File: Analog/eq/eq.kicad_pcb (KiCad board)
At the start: 2 copper layers, 39 parts, among them J2 NMJ4HCD2, J3 NMJ6HCD2, U1 NJM4580, U3 SA5532

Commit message: EQ pcb started and Analog file re-org
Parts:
- moved J3 70.9 mm to (72.6, 69.9)
- moved J2 38.7 mm to (179.6, 64.9)
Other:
- board text added: "INPUT"
- board text added: "OUTPUT"
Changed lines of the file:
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@@
 	(footprint "Connector_Audio:Jack_6.35mm_Neutrik_NMJ6HCD2_Horizontal"
 		(layer "F.Cu")
-		(at 143.385 72.305)
+		(at 72.565 69.885)
 		(descr "M Series, 6.35mm (1/4in) stereo jack, switched, with chrome ferrule and straight PCB pins, https://www.neutrik.com/en/product/nmj6hcd2")
 		(tags "neutrik jack m")
@@
 	(footprint "Connector_Audio:Jack_6.35mm_Neutrik_NMJ4HCD2_Horizontal"
 		(layer "F.Cu")
-		(at 143.385 51.025)
+		(at 179.565 64.885)
 		(descr "M Series, 6.35mm (1/4in) mono jack, switched, with chrome ferrule and straight PCB pins, https://www.neutrik.com/en/product/nmj4hcd2")
 		(tags "neutrik jack m")
@@
 		)
 	)
+	(gr_text "INPUT"
+		(at 78 64 0)
+		(layer "F.SilkS")
+		(effects
+			(font
+				(size 1 1)
+				(thickness 0.1)
+			)
+			(justify left bottom)
+		)
+	)
+	(gr_text "OUTPUT"
+		(at 183 59 0)
+		(layer "F.SilkS")
+		(effects
+			(font
+				(size 1 1)
+				(thickness 0.1)
+			)
+			(justify left bottom)
+		)
+	)

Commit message: EQ pcb done
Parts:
- added BT1: Battery, Connector_PinHeader_2.54mm:PinHeader_1x02_P2.54mm_Vertical, F.Cu at (233.7, 154.6)
- moved R1 157.4 mm to (226.0, 145.0), turned to 180 degrees
- moved R3 146.9 mm to (215.8, 149.0)
- moved R5 146.2 mm to (226.0, 141.0), turned to 180 degrees
- moved R2 144.0 mm to (212.5, 144.5), turned to 180 degrees
- moved HIGH1 137.7 mm to (247.9, 112.4), turned to 90 degrees
- moved R15 137.3 mm to (236.7, 120.8)
- moved R11 130.9 mm to (226.1, 126.5), turned to 180 degrees
- moved R14 129.6 mm to (226.1, 133.5), turned to 180 degrees
- moved R4 123.2 mm to (200.6, 134.0), turned to 180 degrees
- moved J3 121.0 mm to (170.4, 141.1), turned to 180 degrees
- moved R13 119.9 mm to (215.9, 130.0)
- moved D1 119.0 mm to (229.5, 144.9), turned to -90 degrees
- moved R8 118.7 mm to (196.6, 148.0), turned to 180 degrees
- moved R9 111.2 mm to (200.6, 130.5), turned to 180 degrees
- moved RPD1 108.7 mm to (202.3, 148.0)
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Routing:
- net Net-(C7-Pad2): track 0.00 -> 113.5 mm
- net Net-(C9-Pad1): track 0.00 -> 68.9 mm
- net Net-(C4-Pad2): track 0.00 -> 60.5 mm
- net VB: track 0.00 -> 60.0 mm
- net Net-(C2-Pad2): track 0.00 -> 58.9 mm
- net Net-(C8-Pad1): track 0.00 -> 53.5 mm
- net Net-(C11-Pad2): track 0.00 -> 46.0 mm
- net VA: track 0.00 -> 44.0 mm
- net Net-(C13-Pad2): track 0.00 -> 35.6 mm
- net Net-(C12-Pad1): track 0.00 -> 30.9 mm
- net Net-(C14-Pad1): track 0.00 -> 26.4 mm
- net Net-(C10-Pad2): track 0.00 -> 26.2 mm
- net Net-(C5-Pad2): track 0.00 -> 25.9 mm
- net Net-(U1A--): track 0.00 -> 24.5 mm
- net Net-(C15-Pad2): track 0.00 -> 23.9 mm
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- added copper zone on B.Cu, net GND
- added copper zone on F.Cu, net GND
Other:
- board outline added: 100 x 69 mm

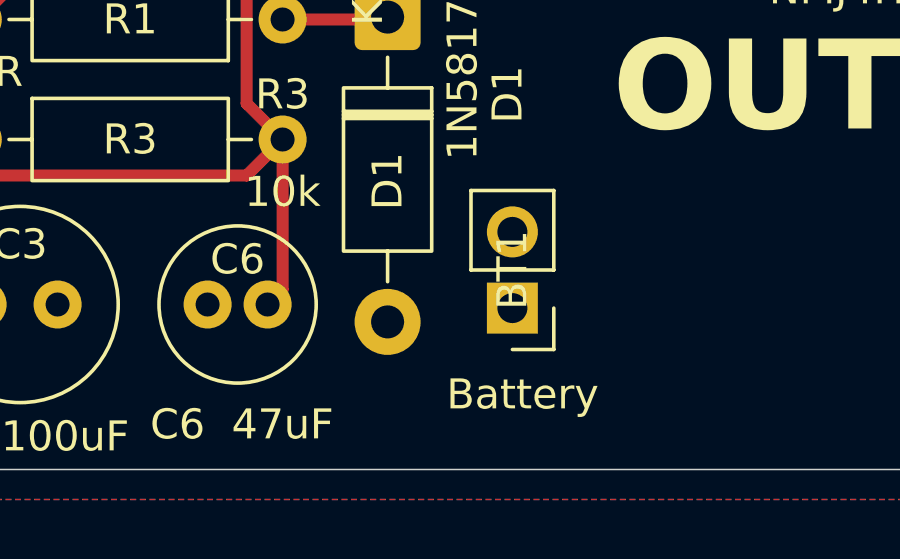
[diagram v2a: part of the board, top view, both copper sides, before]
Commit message: fixed battery trace
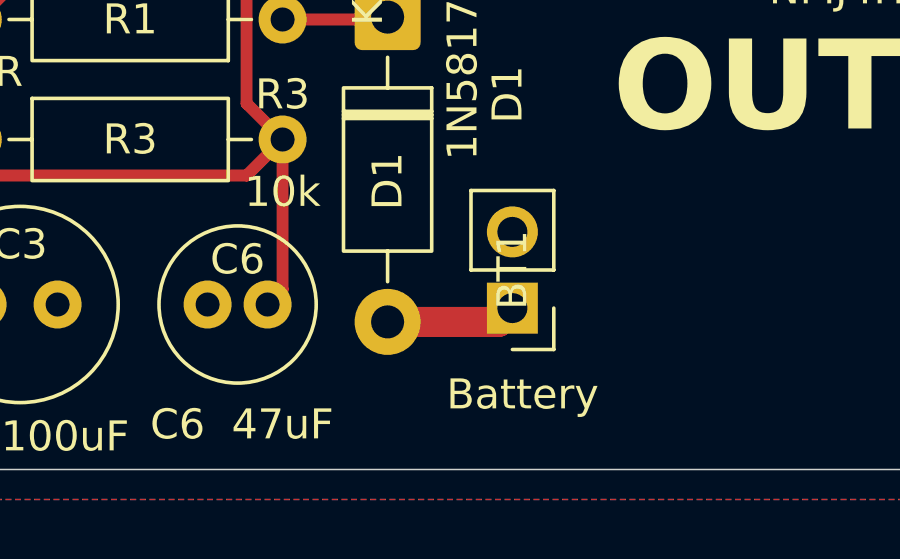
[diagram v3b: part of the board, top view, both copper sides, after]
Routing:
- net +9V: track 0.00 -> 4.35 mm
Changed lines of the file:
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@@
+	)
+	(segment
+		(start 229.5 155.08)
+		(end 233.2 155.08)
+		(width 1)
+		(layer "F.Cu")
+		(net "+9V")
+	)
+	(segment
+		(start 233.2 155.08)
+		(end 233.66 154.62)
+		(width 1)
+		(layer "F.Cu")
+		(net "+9V")
 	)
 	(segment
